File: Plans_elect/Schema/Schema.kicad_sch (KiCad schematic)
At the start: 23 parts, among them J1 Conn_01x22, J2 Conn_01x22, J3 Conn_01x10, J4 Conn_01x14, SW1 RotaryEncoder_Switch, SW2 RotaryEncoder_Switch, SW3 RotaryEncoder

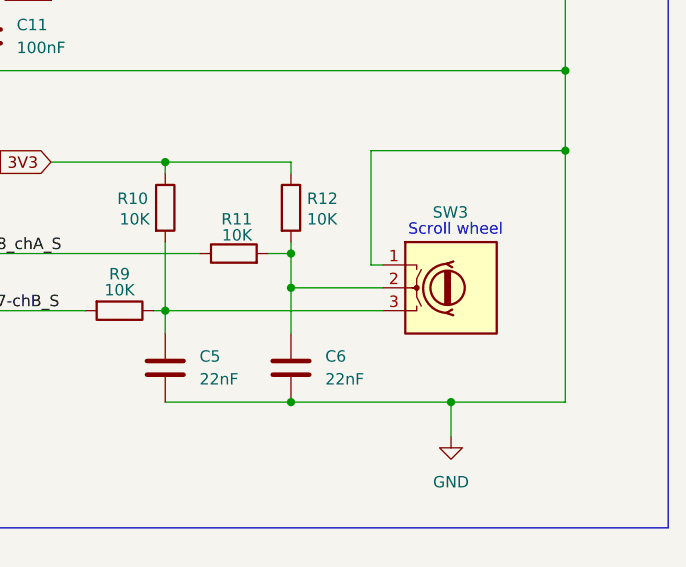
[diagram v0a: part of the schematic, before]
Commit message: Plan elect finit
il y a 16 erreurs mais les 16 c'est sur le fait que jai essayer de faire mon propre footprint pis ca fait nimporte quoi
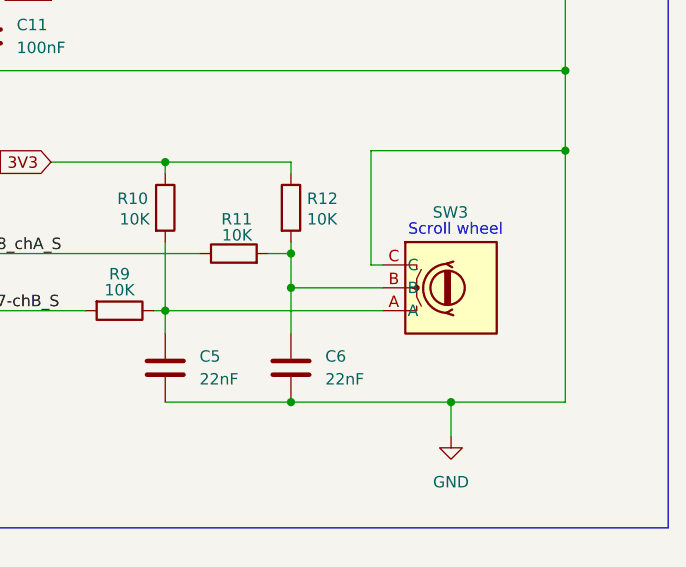
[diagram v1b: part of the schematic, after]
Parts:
- J1, J2: footprint Connector_PinHeader_1.00mm:PinHeader_1x22_P1.00mm_Vertical -> Connector_PinHeader_2.54mm:PinHeader_1x22_P2.54mm_Vertical
- J3: footprint Connector_PinHeader_1.00mm:PinHeader_1x10_P1.00mm_Vertical -> Connector_PinHeader_2.54mm:PinHeader_1x10_P2.54mm_Vertical
- J4: footprint Connector_PinHeader_1.00mm:PinHeader_1x14_P1.00mm_Vertical -> Connector_PinHeader_2.54mm:PinHeader_1x14_P2.54mm_Vertical
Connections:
- net GND: now also SW3.C; no longer SW3.1
- net at C5.1, R10.2, R9.1: now also SW3.A; no longer SW3.3
- net at C6.1, R11.2, R12.2: now also SW3.B; no longer SW3.2
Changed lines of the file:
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@@
 			)
 		)
-		(property "Footprint" "Connector_PinHeader_1.00mm:PinHeader_1x22_P1.00mm_Vertical"
+		(property "Footprint" "Connector_PinHeader_2.54mm:PinHeader_1x22_P2.54mm_Vertical"
 			(at 119.38 72.39 0)
 			(effects
@@
 			)
 		)
-		(pin "2"
-		)
-		(pin "1"
-		)
-		(pin "3"
+		(pin "B"
+		)
+		(pin "C"
+		)
+		(pin "A"
 		)
 		(instances
@@
 			)
 		)
-		(property "Footprint" "Connector_PinHeader_1.00mm:PinHeader_1x22_P1.00mm_Vertical"
+		(property "Footprint" "Connector_PinHeader_2.54mm:PinHeader_1x22_P2.54mm_Vertical"
 			(at 127 74.93 0)
 			(effects
@@
 			)
 		)
-		(property "Footprint" "Connector_PinHeader_1.00mm:PinHeader_1x14_P1.00mm_Vertical"
+		(property "Footprint" "Connector_PinHeader_2.54mm:PinHeader_1x14_P2.54mm_Vertical"
 			(at 115.57 154.94 0)
 			(effects
@@
 			)
 		)
-		(property "Footprint" "Connector_PinHeader_1.00mm:PinHeader_1x10_P1.00mm_Vertical"
+		(property "Footprint" "Connector_PinHeader_2.54mm:PinHeader_1x10_P2.54mm_Vertical"
 			(at 48.26 127 0)
 			(effects
